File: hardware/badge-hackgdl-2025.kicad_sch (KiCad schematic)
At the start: 53 parts, among them J1 ADDON, J2 Battery, P1 USB_C_Plug_USB2.0, Q1 DMG3415U-7, Q2 MMBT2222A, SW1 ON, SW2 RESET, SW3 BOOT, SW4 LEFT, SW5 BACK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

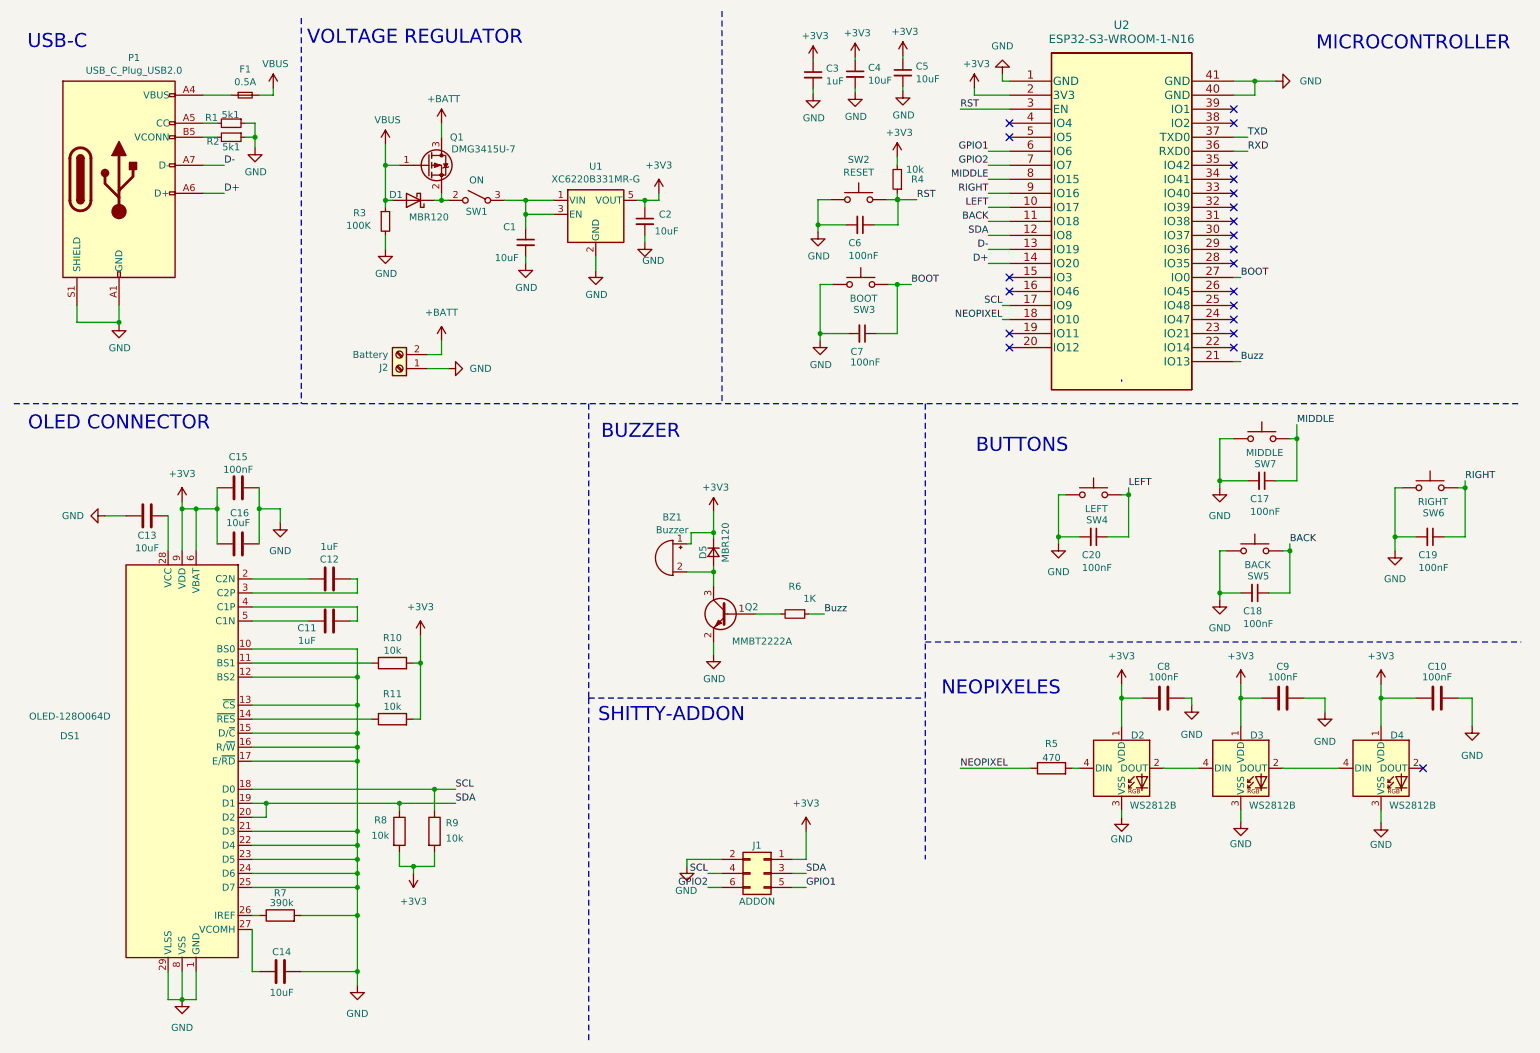
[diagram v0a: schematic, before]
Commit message: feat(hw): add routes in pcb
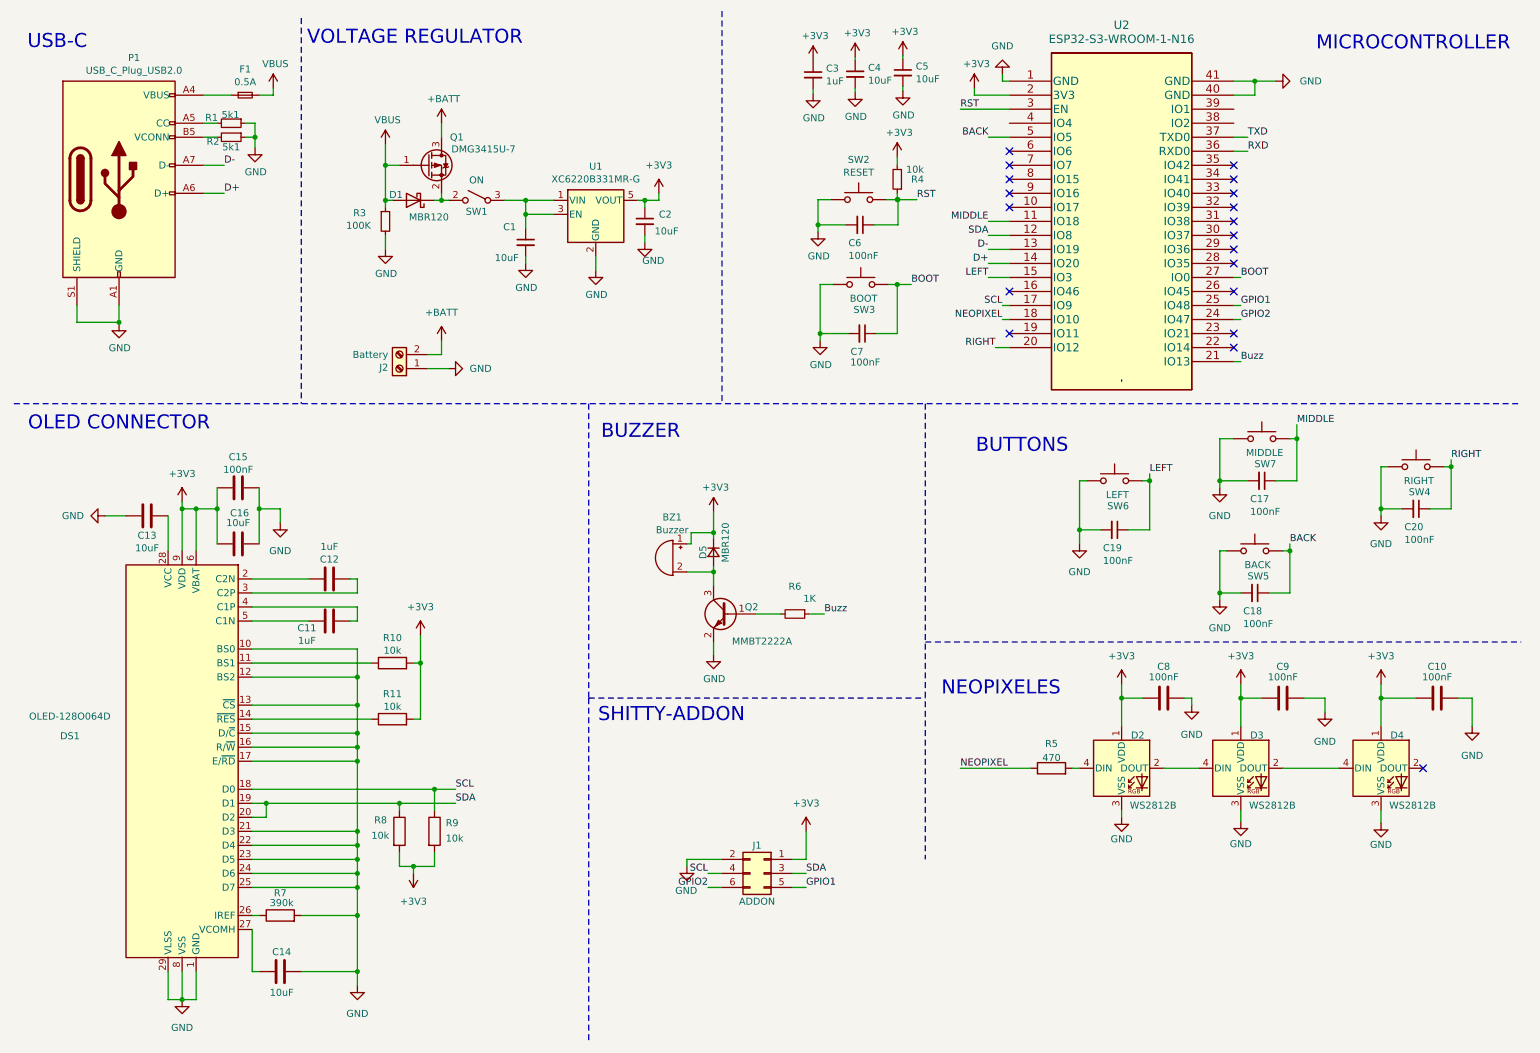
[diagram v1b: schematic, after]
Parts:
- DS1: footprint Footprints:ssd1306_oled_conn -> Footprints:ssd1306_oled_conn_through_the_oled
- SW4: value LEFT -> RIGHT
- SW6: value RIGHT -> LEFT
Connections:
- net BACK: now also U2.5 (IO5); no longer U2.11 (IO18)
- net GPIO1: now also U2.25 (IO48); no longer U2.6 (IO6)
- net GPIO2: now also U2.24 (IO47); no longer U2.7 (IO7)
- net LEFT: now also C19.1, SW6.2, U2.15 (IO3); no longer C20.1, SW4.2, U2.10 (IO17)
- net MIDDLE: now also U2.11 (IO18); no longer U2.8 (IO15)
- net RIGHT: now also C20.1, SW4.2, U2.20 (IO12); no longer C19.1, SW6.2, U2.9 (IO16)
- no-connect marks 22 -> 19
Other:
- moved on the sheet: C19, C20, SW4, SW6

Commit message: feat(hw): change ON/OFF switch
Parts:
- C1, C2, D1, Q1, R3, U1: Proveedor JLCPCB -> (none)
- C10, C17, C18, C19, C20, C3, C4, C5, C6, C7, C8, C9, D2, D3, D4, R4, SW2, SW3, SW4, SW5, SW6, SW7: Proveedor LCSC -> (none)
- J1: Proveedor DIGIKEY -> (none)
- SW1: footprint Footprints:MSK12C02 -> Footprints:JS102011SAQN; LCSC# C431540 -> C221660; Proveedor JLCPCB -> (none); provedor MOUSER -> LCSC
- U2: MOUSER# ESP32-S3-WROOM-1-N8R2 -> (none); Proveedor MOUSER -> (none)

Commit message: feat(hw): add labels
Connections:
- net RXD: no longer names the net of U2.36 (RXD0)
- net TXD: no longer names the net of U2.37 (TXD0)
- no-connect marks 19 -> 23
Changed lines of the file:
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@@
+	)
+	(no_connect
+		(at 232.41 31.75)
 	)
 	(no_connect
@@
 	)
 	(no_connect
+		(at 232.41 36.83)
+	)
+	(no_connect
 		(at 191.77 41.91)
 	)
@@
 	)
 	(no_connect
+		(at 232.41 34.29)
+	)
+	(no_connect
 		(at 232.41 46.99)
 	)
@@
 	)
 	(no_connect
+		(at 232.41 29.21)
+	)
+	(no_connect
 		(at 232.41 49.53)
 	)
@@
 		)
 	)
-	(wire
-		(pts
-			(xy 232.41 36.83) (xy 234.95 36.83)
-		)
-		(stroke
-			(width 0)
-			(type default)
-		)
-	)
 	(polyline
 		(pts
@@
 		(pts
 			(xy 88.9 45.72) (xy 90.17 45.72)
-		)
-		(stroke
-			(width 0)
-			(type default)
-		)
-	)
-	(wire
-		(pts
-			(xy 232.41 34.29) (xy 234.95 34.29)
 		)
 		(stroke
@@
 		)
 	)
-	(label "RXD"
-		(at 234.95 36.83 0)
-		(effects
-			(font
-				(size 1.27 1.27)
-			)
-			(justify left bottom)
-		)
-	)
 	(label "RIGHT"
 		(at 189.23 72.39 180)
@@
 		)
 	)
-	(label "TXD"
-		(at 234.95 34.29 0)
-		(effects
-			(font
-				(size 1.27 1.27)
-			)
-			(justify left bottom)
-		)
-	)

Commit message: feat(hw): change size of pads in the oled footprint
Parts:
- F1: value 0.5A -> 1A; LCSC# C182438 -> C151139; manf# 06D0750D -> (none)
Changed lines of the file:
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@@
 			)
 		)
-		(property "Value" "0.5A"
+		(property "Value" "1A"
 			(at 53.34 24.2824 0)
 			(effects
@@
 			)
 		)
-		(property "manf#" "06D0750D"
+		(property "manf#" ""
 			(at 53.34 26.67 0)
 			(effects
@@
 			)
 		)
-		(property "LCSC#" " C182438"
+		(property "LCSC#" "C151139"
 			(at 53.34 26.67 0)
 			(effects

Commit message: refactor(hw): move buttons
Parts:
- D2, D3, D4: manf# WS2812B-Mini -> (none)
- P1: manf# TYPE-C-31-M-31 -> (none)
- R1, R2: manf# ERJ3RBD5101V -> (none)
- R5: manf# RTT03471JTP -> (none)
- SW2, SW3, SW4, SW5, SW6, SW7: LCSC# C455281 -> C318884
- U1: manf# XC6220B331MR-G -> (none)
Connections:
- no-connect marks 23 -> 24
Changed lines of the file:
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@@
 	)
 	(no_connect
+		(at 191.77 31.75)
+	)
+	(no_connect
 		(at 232.41 54.61)
 	)
@@
 			)
 		)
-		(property "manf#" "WS2812B-Mini"
+		(property "manf#" ""
 			(at 233.68 148.59 0)
 			(effects
@@
 			)
 		)
-		(property "manf#" "WS2812B-Mini"
+		(property "manf#" ""
 			(at 259.08 148.59 0)
 			(effects
@@
 			)
 		)
-		(property "manf#" "ERJ3RBD5101V"
+		(property "manf#" ""
 			(at 50.8 34.29 0)
 			(effects
@@
 			)
 		)
-		(property "LCSC#" "C455281"
+		(property "LCSC#" "C318884"
 			(at 237.49 88.9 0)
 			(effects
@@
 			)
 		)
-		(property "manf#" "XC6220B331MR-G "
+		(property "manf#" ""
 			(at 116.84 48.26 0)
 			(effects
@@
 			)
 		)
-		(property "LCSC#" "C455281"
+		(property "LCSC#" "C318884"
 			(at 265.43 93.98 0)
 			(effects
@@
 			)
 		)
-		(property "LCSC#" "C455281"
+		(property "LCSC#" "C318884"
 			(at 236.22 109.22 0)
 			(effects
@@
 			)
 		)
-		(property "LCSC#" "C455281"
+		(property "LCSC#" "C318884"
 			(at 210.82 96.52 0)
 			(effects
@@
 			)
 		)
-		(property "manf#" "WS2812B-Mini"
+		(property "manf#" ""
 			(at 212.09 148.59 0)
 			(effects
@@
 			)
 		)
-		(property "manf#" "TYPE-C-31-M-31"
+		(property "manf#" ""
 			(at 30.48 41.91 0)
 			(effects
@@
 			)
 		)
-		(property "manf#" "RTT03471JTP"
+		(property "manf#" ""
 			(at 199.39 148.59 0)
 			(effects
@@
 			)
 		)
-		(property "LCSC#" "C455281"
+		(property "LCSC#" "C318884"
 			(at 164.846 60.96 0)
 			(effects
@@
 			)
 		)
-		(property "manf#" "ERJ3RBD5101V"
+		(property "manf#" ""
 			(at 50.8 31.75 0)
 			(effects
@@
 			)
 		)
-		(property "LCSC#" "C455281"
+		(property "LCSC#" "C318884"
 			(at 164.465 45.593 0)
 			(effects

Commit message: feat(hw): add space between buttons
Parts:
- BZ1: provedor MOUSER -> JLCPCB
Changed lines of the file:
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@@
 			)
 		)
-		(property "provedor" "MOUSER"
+		(property "provedor" "JLCPCB"
 			(at 130.81 110.49 0)
 			(effects

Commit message: fix(hw): change gpio pins for addon connector
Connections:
- net Buzz: now also U2.19 (IO11); no longer U2.21 (IO13)
- net GPIO1: now also U2.22 (IO14); no longer U2.25 (IO48)
- net GPIO2: now also U2.21 (IO13); no longer U2.24 (IO47)
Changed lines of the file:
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@@
+	)
+	(no_connect
+		(at 232.41 64.77)
 	)
 	(no_connect
@@
 	)
 	(no_connect
+		(at 232.41 67.31)
+	)
+	(no_connect
 		(at 191.77 36.83)
 	)
@@
 	)
 	(no_connect
-		(at 191.77 69.85)
-	)
-	(no_connect
 		(at 232.41 29.21)
 	)
@@
 	)
 	(no_connect
-		(at 232.41 72.39)
-	)
-	(no_connect
 		(at 232.41 39.37)
 	)
@@
 	(wire
 		(pts
+			(xy 232.41 72.39) (xy 233.68 72.39)
+		)
+		(stroke
+			(width 0)
+			(type default)
+		)
+	)
+	(wire
+		(pts
 			(xy 54.61 152.4) (xy 87.63 152.4)
 		)
@@
 	(wire
 		(pts
+			(xy 190.5 69.85) (xy 191.77 69.85)
+		)
+		(stroke
+			(width 0)
+			(type default)
+		)
+	)
+	(wire
+		(pts
 			(xy 169.926 60.96) (xy 171.45 60.96)
 		)
@@
 	(wire
 		(pts
+			(xy 232.41 74.93) (xy 233.68 74.93)
+		)
+		(stroke
+			(width 0)
+			(type default)
+		)
+	)
+	(wire
+		(pts
 			(xy 125.73 52.07) (xy 125.73 53.34)
 		)
@@
 	(wire
 		(pts
-			(xy 232.41 64.77) (xy 233.68 64.77)
-		)
-		(stroke
-			(width 0)
-			(type default)
-		)
-	)
-	(wire
-		(pts
 			(xy 233.68 156.21) (xy 233.68 158.242)
 		)
@@
 	(wire
 		(pts
-			(xy 232.41 67.31) (xy 233.68 67.31)
-		)
-		(stroke
-			(width 0)
-			(type default)
-		)
-	)
-	(wire
-		(pts
 			(xy 54.61 132.08) (xy 73.66 132.08)
 		)
@@
 			(width 0)
 			(type dash)
-		)
-	)
-	(wire
-		(pts
-			(xy 232.41 74.93) (xy 233.68 74.93)
-		)
-		(stroke
-			(width 0)
-			(type default)
 		)
 	)
@@
 	)
 	(label "Buzz"
-		(at 233.68 74.93 0)
-		(effects
-			(font
-				(size 1.27 1.27)
-			)
-			(justify left bottom)
+		(at 190.5 69.85 180)
+		(effects
+			(font
+				(size 1.27 1.27)
+			)
+			(justify right bottom)
 		)
 	)
@@
 	)
 	(label "GPIO1"
-		(at 233.68 64.77 0)
+		(at 233.68 72.39 0)
 		(effects
 			(font
@@
 	)
 	(label "GPIO2"
-		(at 233.68 67.31 0)
-		(effects
-			(font
+		(at 233.68 74.93 0)
+		(effects
+			(font

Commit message: fix(hw): change left button to gpio 17
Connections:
- net LEFT: now also U2.10 (IO17); no longer U2.15 (IO3)
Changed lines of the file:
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@@
-	)
-	(no_connect
-		(at 191.77 46.99)
 	)
 	(no_connect
@@
 	)
 	(no_connect
+		(at 191.77 59.69)
+	)
+	(no_connect
 		(at 232.41 39.37)
 	)
@@
 		)
 	)
+	(wire
+		(pts
+			(xy 189.23 46.99) (xy 191.77 46.99)
+		)
+		(stroke
+			(width 0)
+			(type default)
+		)
+	)
 	(polyline
 		(pts
@@
 		(pts
 			(xy 73.66 121.92) (xy 72.39 121.92)
-		)
-		(stroke
-			(width 0)
-			(type default)
-		)
-	)
-	(wire
-		(pts
-			(xy 187.96 59.69) (xy 191.77 59.69)
 		)
 		(stroke
@@
 	)
 	(label "LEFT"
-		(at 187.96 59.69 180)
+		(at 189.23 46.99 180)
 		(effects
 			(font
